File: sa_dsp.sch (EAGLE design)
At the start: 379 parts, among them CN1 uSD, CN2 MINI B USB, CN3 2X5 HEADER, CN4 MINI B USB, CN5 USB A, CN6 MINI B USB, Q3 2N7002, Q4 2N7002, SW1 1825910-7, U1 PGA2311, U10 LME49720, U11 PGA2311, U12 LME49720, U13 LME49720, U14 PCM1754, U15 LME49720, U16 PGA2311, U17 LME49720, U18 LME49720, U19 PCM1754, U2 LM317, U20 LME49720, U21 7 SEG, U22 74HC164A, U23 PCM2707, U24 PCM2707, U25 7 SEG, U26 74HC164A, U27 LM337, U28 LM317, U29 7 SEG, U3 OSD3358-512M-BSM, U30 74HC164A, U31 100MHz, U32 USBLC6-2SC6, U33 FT230X, U34 USBLC6-2SC6, U35 USBLC6-2SC6, U36 USBLC6-2SC6, U37 2 PORT HUB, U39 LM22670, U4 LME49720, U5 LME49720, U6 10CL016YF484C6G, U7 7 SEG, U8 74HC164A, U9 PCM1754

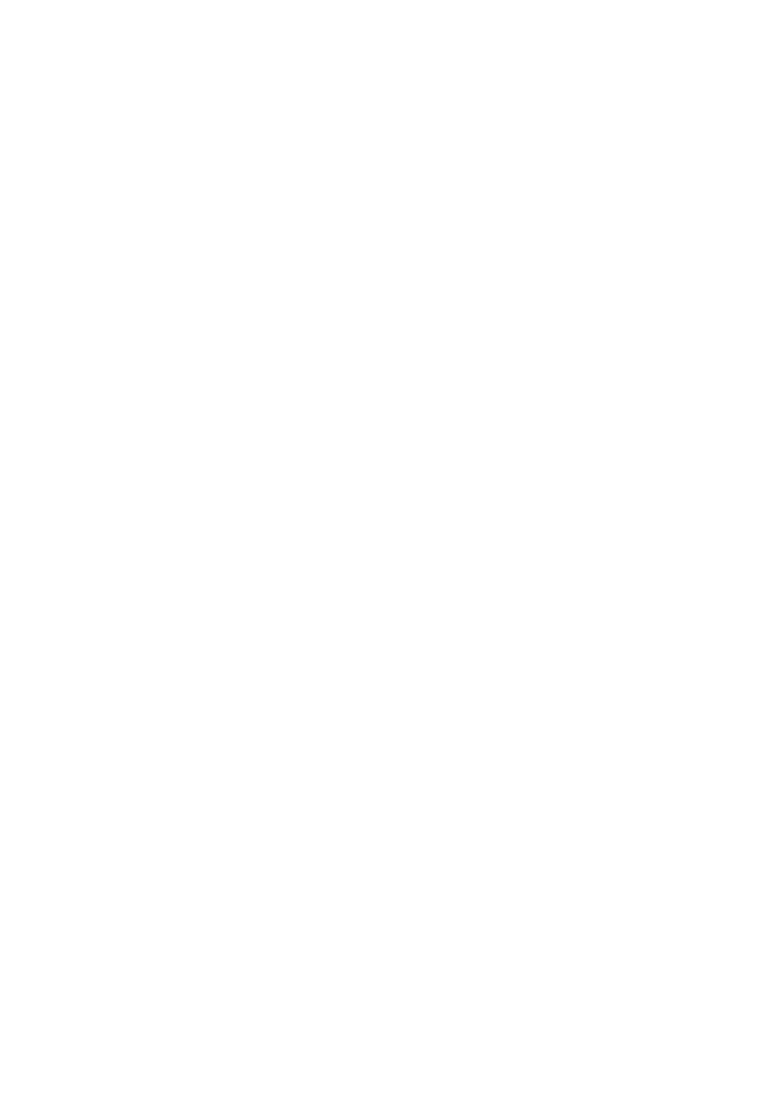
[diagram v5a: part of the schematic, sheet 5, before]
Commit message: PSUs done for the FPGA
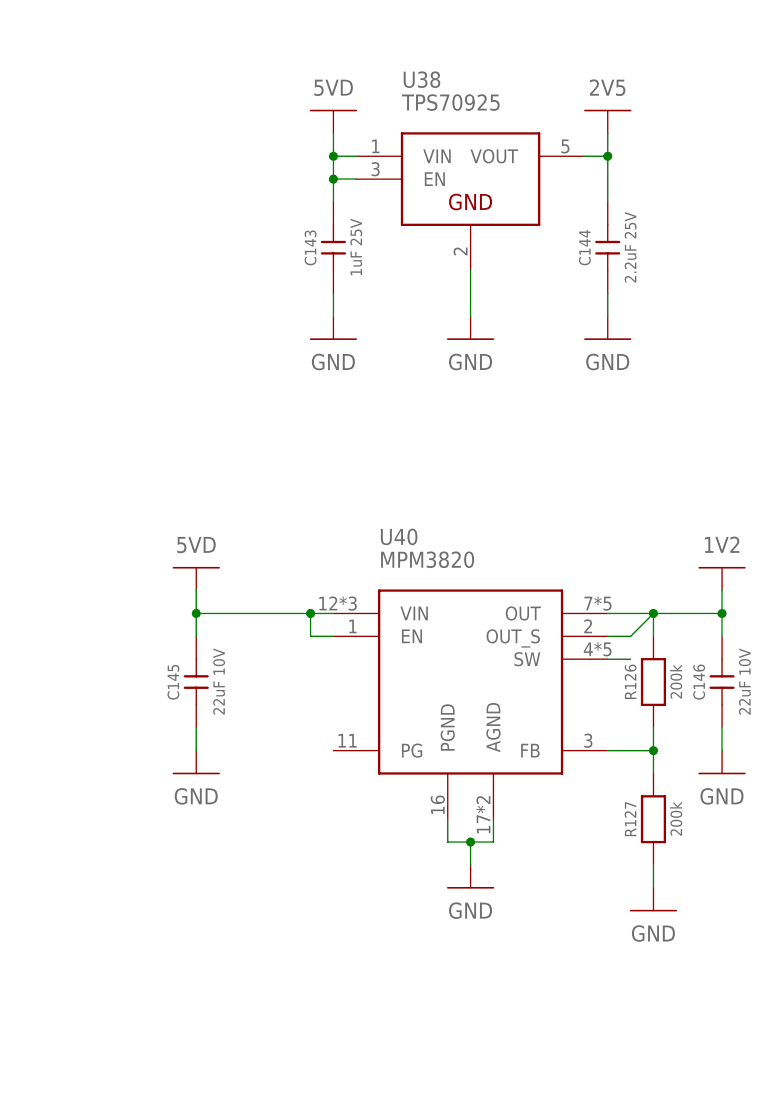
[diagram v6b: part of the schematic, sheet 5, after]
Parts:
- added C143: 1uF 25V, CAPACITORS:CL10A105KA8NNNC
- added C144: 2.2uF 25V, CAPACITORS:GRM188R61E225KA12D
- added C145, C146: 22uF 10V, CAPACITORS:CL31B226MPHNNNE
- added R126, R127: 200k, r_0603:ERJ3EKF2003V
- added U38: TPS70925, ICs:TPS70925DBVR
- added U40: MPM3820, ICs:MPM3820GQV-Z
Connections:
- new net N$207: U40.SW
- new net N$210: R126.1, R127.2, U40.FB
- net 1V2: now also C146.2, R126.2, U40.OUT, U40.OUT_S
- net 2V5: now also C144.2, U38.VOUT
- net 5VD: now also C143.2, C145.2, U38.EN, U38.VIN, U40.EN, U40.VIN
- net DAC0_I2S_BCLK: now also U6.B5_IO13
- net DAC0_I2S_DATA: now also U6.B5_IO12
- net DAC0_I2S_LRCLK: now also U6.B5_IO21
- net DAC0_I2S_SCLK: now also U6.B5_IO20
- net DAC0_MUTE: now also U6.B5_IO24
- net DAC1_I2S_BCLK: now also U6.B5_IO31
- net DAC1_I2S_DATA: now also U6.B5_IO38
- net DAC1_I2S_LRCLK: now also U6.B5_IO37
- net DAC1_I2S_SCLK: now also U6.B5_IO40
- net DAC1_MUTE: now also U6.B5_IO39
- net DAC2_I2S_BCLK: now also U6.B6_IO18
- net DAC2_I2S_DATA: now also U6.B6_IO19
- net DAC2_I2S_LRCLK: now also U6.B6_IO22
- net DAC2_I2S_SCLK: now also U6.B6_IO23
- net DAC2_MUTE: now also U6.B6_IO27
- net GND: now also C143.1, C144.1, C145.1, C146.1, R127.1, U38.GND, U40.AGND, U40.PGND
- net PGA0_!CS: now also U6.B5_IO32
- net PGA0_!MUTE: now also U6.B5_IO23
- net PGA0_SCLK: now also U6.B5_IO29
- net PGA0_SDI: now also U6.B5_IO28
- net PGA1_!CS: now also U6.B6_IO17
- net PGA1_!MUTE: now also U6.B6_IO11
- net PGA1_SCLK: now also U6.B6_IO12
- net PGA1_SDI: now also U6.B6_IO16
- net PGA2_!CS: now also U6.B6_IO36
- net PGA2_!MUTE: now also U6.B6_IO28
- net PGA2_SCLK: now also U6.B6_IO31
- net PGA2_SDI: now also U6.B6_IO32

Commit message: Progress
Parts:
- added C159, C160: 22uF 10V, CAPACITORS:CL31B226MPHNNNE
- added D10, D7: CG0603MLC, DIODES:CG0603MLC-12LE
- added D11, D9: B0540W, DIODES:B0540W
- added Q1, Q2: 2N7002, TRANSISTORs:2N7002P,215
- added R129, R131, R132: 100k, r_0603:ERJ3EKF1003V
- added R130: 22k, r_0603:ERJ3EKF2202V
- added TP10, TP11, TP12, TP8, TP9: TEST_POINT_SQUARE, MISC:TEST_POINT_SQUARE
- added TP13, TP14, TP15, TP16: 2MM_TEST_POINT, MISC:2MM_TEST_POINT
- added U41: MPM3820, ICs:MPM3820GQV-Z
- R126, R127: value 200k -> 22k; device r_0603:ERJ3EKF2003V -> r_0603:ERJ3EKF2202V
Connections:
- new net IO_AUDIO_RLY_EN: Q2.G, R132.2
- new net N$211: R129.1, R130.2, U41.FB
- new net N$237: D10.A1, D11.A, Q2.D, TP16.P$1
- new net PSU_AMP_PWR_EN: Q1.G, R131.2
- net 15VA+_UNREG: now also TP10.P$1
- net 15VA-_UNREG: now also TP12.P$1
- net 15VD_UNREG: now also D11.K, D9.K, TP13.P$1, TP15.P$1, TP8.P$1
- net 3V3: now also C160.2, R129.2, U41.OUT, U41.OUT_S
- net 5VD: now also C159.2, U41.EN, U41.VIN
- net AGND: now also TP11.P$1
- net GND: now also C159.1, C160.1, D10.A, D7.A, Q1.S, Q2.S, R130.1, R131.1, R132.1, TP9.P$1, U41.AGND, U41.PGND
- net N$207: now also D7.A1, D9.A, Q1.D, TP14.P$1; no longer U40.SW
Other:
- moved on the sheet: C145, C146, R126, R127, U40

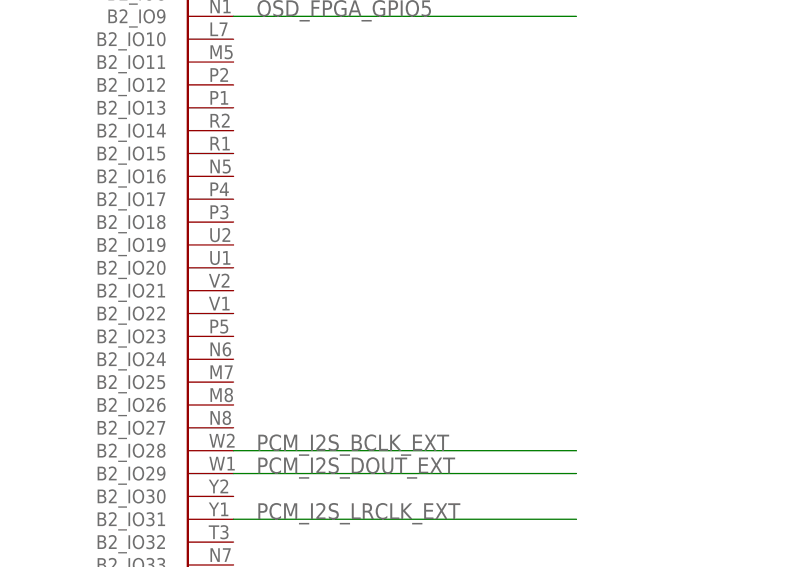
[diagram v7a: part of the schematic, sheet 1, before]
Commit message: FPGA config needs check, full review, DRC, airwires and architecture review needed
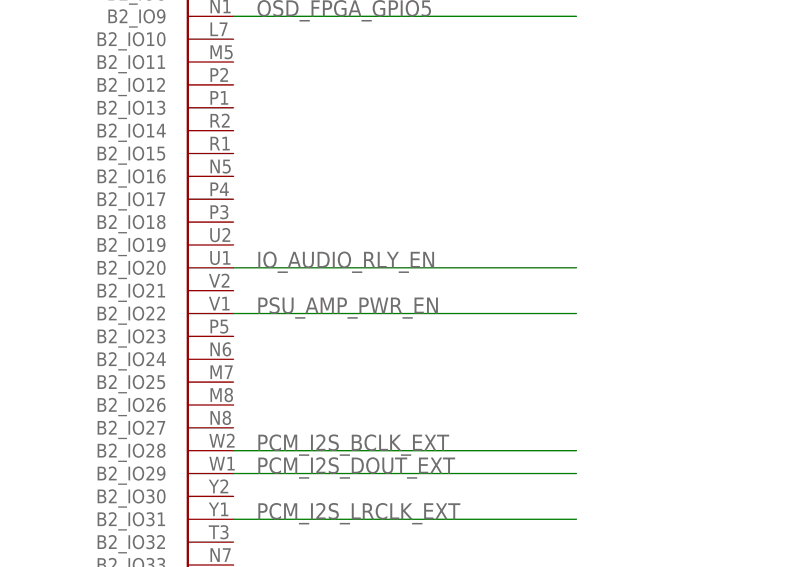
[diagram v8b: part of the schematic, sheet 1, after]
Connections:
- net IO_AUDIO_RLY_EN: now also U6.B2_IO20
- net PSU_AMP_PWR_EN: now also U6.B2_IO22
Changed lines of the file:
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@@
 <label x="452.12" y="360.68" size="1.778" layer="95"/>
+</segment>
+<segment>
+<pinref part="U6" gate="G$1" pin="B2_IO22"/>
+<wire x1="312.42" y1="340.36" x2="350.52" y2="340.36" width="0.1524" layer="91"/>
+<label x="314.96" y="340.36" size="1.778" layer="95"/>
 </segment>
 </net>
@@
 <label x="452.12" y="304.8" size="1.778" layer="95"/>
 </segment>
+<segment>
+<pinref part="U6" gate="G$1" pin="B2_IO20"/>
+<wire x1="312.42" y1="345.44" x2="350.52" y2="345.44" width="0.1524" layer="91"/>
+<label x="314.96" y="345.44" size="1.778" layer="95"/>
+</segment>
 </net>
